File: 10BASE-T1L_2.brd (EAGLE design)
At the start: 60.8 x 75 mm, 163 parts, among them J1 10104110-0001LF, J2 A-2004-2-4-LPS-N-R, J3 TBL009-254-03GY-2GY, J4 TBL009-254-02GY-2GY, T1 ALT4532M-201-T001, T4 H1102NLT, U1 DP83TD510ERHBR, U2 DP83822IRHBR, U3 CO32H4-25.000-33GDTST, U4 LMR38020SDDAR, U5 SN74LVC1G17DCKR, U6 SN74LVC1G17DCKR

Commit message: adding reset cap
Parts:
- added C61: 10nF, ruark2:0402_INDUCTOR
- R68: value 100k -> 115k
- R69: value 24.9k -> 49.9k
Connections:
- net !RST: now also C61.P$1
- net GND: now also C61.P$2
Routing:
- net GND: track 73.3 -> 74.1 mm, vias 92 -> 97
- net !RST: track 24.1 -> 24.6 mm
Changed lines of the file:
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@@
 <attribute name="VALUE" x="11.684" y="11.176" size="1.27" layer="27"/>
 </element>
-<element name="R68" library="ruark2" package="0603" value="100k" x="5.842" y="31.496" smashed="yes" rot="R90">
+<element name="R68" library="ruark2" package="0603" value="115k" x="5.842" y="31.496" smashed="yes" rot="R90">
 <attribute name="NAME" x="5.08" y="30.226" size="1.016" layer="25" font="vector" ratio="10" rot="R90"/>
 <attribute name="VALUE" x="7.62" y="30.226" size="1.016" layer="27" font="vector" rot="R90"/>
 </element>
-<element name="R69" library="ruark2" package="0603" value="24.9k" x="5.842" y="34.798" smashed="yes" rot="R270">
+<element name="R69" library="ruark2" package="0603" value="49.9k" x="5.842" y="34.798" smashed="yes" rot="R270">
 <attribute name="NAME" x="5.08" y="33.782" size="1.016" layer="25" font="vector" ratio="10" rot="R90"/>
 <attribute name="VALUE" x="4.064" y="36.068" size="1.016" layer="27" font="vector" rot="R270"/>
@@
 </element>
 <element name="C30" library="ruark2" package="0402_INDUCTOR" value="47pF" x="43.434" y="15.748" smashed="yes" rot="R270">
-<attribute name="NAME" x="43.942" y="16.51" size="1.016" layer="25" font="vector" ratio="10" rot="R270"/>
+<attribute name="NAME" x="42.926" y="13.97" size="1.016" layer="25" font="vector" ratio="10" rot="R270"/>
 </element>
 <element name="L6" library="ruark2" package="TMPC0603H" value="22uH" x="6.858" y="19.812" smashed="yes" rot="R90">
@@
 <element name="C60" library="ruark2" package="0402_INDUCTOR" value="0.1uF" x="45.974" y="10.16" smashed="yes" rot="R90">
 <attribute name="NAME" x="47.498" y="8.89" size="1.016" layer="25" font="vector" rot="R90"/>
+</element>
+<element name="C61" library="ruark2" package="0402_INDUCTOR" value="10nF" x="42.926" y="27.94" smashed="yes" rot="R180">
+<attribute name="NAME" x="43.688" y="27.432" size="1.016" layer="25" font="vector" rot="R180"/>
 </element>
 </elements>
@@
 <wire x1="28.448" y1="22.098" x2="27.94" y2="22.606" width="0.4064" layer="1"/>
 <polygon width="0.1524" layer="1">
-<vertex x="6.604" y="68.58"/>
-<vertex x="6.604" y="54.356"/>
-<vertex x="3.048" y="54.356"/>
-<vertex x="3.048" y="68.58"/>
+<vertex x="6.604" y="69.342"/>
+<vertex x="6.604" y="53.086"/>
+<vertex x="3.048" y="53.086"/>
+<vertex x="3.048" y="69.342"/>
 </polygon>
 <contactref element="TP1" pad="P$1"/>
@@
 <wire x1="36.83" y1="7.882" x2="39.408" y2="7.882" width="0.180340625" layer="1"/>
 <wire x1="39.408" y1="7.882" x2="39.512" y2="7.986" width="0.180340625" layer="1"/>
+<contactref element="C61" pad="P$2"/>
+<wire x1="43.426" y1="27.94" x2="44.196" y2="27.94" width="0.180340625" layer="1"/>
+<via x="44.196" y="27.94" extent="1-16" drill="0.3048"/>
+<via x="3.556" y="53.594" extent="1-16" drill="0.3048"/>
+<via x="6.096" y="53.594" extent="1-16" drill="0.3048"/>
+<via x="6.096" y="68.834" extent="1-16" drill="0.3048"/>
+<via x="3.556" y="68.834" extent="1-16" drill="0.3048"/>
 </signal>
 <signal name="N$15">
@@
 <wire x1="45.428575" y1="22.86" x2="45.03674375" y2="23.25183125" width="0.180340625" layer="1"/>
 <wire x1="45.03674375" y1="24.77583125" x2="43.688" y2="26.124575" width="0.180340625" layer="1"/>
-<wire x1="43.688" y1="26.124575" x2="43.688" y2="26.924" width="0.180340625" layer="1"/>
-<via x="43.688" y="26.924" extent="1-16" drill="0.3048"/>
-<wire x1="43.688" y1="26.924" x2="42.418" y2="28.194" width="0.180340625" layer="16"/>
-<wire x1="42.418" y1="33.274" x2="42.418" y2="28.194" width="0.180340625" layer="16"/>
+<wire x1="43.688" y1="26.124575" x2="43.688" y2="26.416" width="0.180340625" layer="1"/>
+<via x="43.688" y="26.416" extent="1-16" drill="0.3048"/>
+<wire x1="43.688" y1="26.416" x2="42.418" y2="27.686" width="0.180340625" layer="16"/>
+<wire x1="42.418" y1="33.274" x2="42.418" y2="27.686" width="0.180340625" layer="16"/>
 <via x="42.418" y="33.274" extent="1-16" drill="0.3048"/>
 <wire x1="42.418" y1="33.274" x2="42.418" y2="34.282" width="0.180340625" layer="1"/>
@@
 <wire x1="46.422" y1="22.348" x2="45.47" y2="22.348" width="0.180340625" layer="1"/>
 <wire x1="45.47" y1="22.348" x2="44.704" y2="23.114" width="0.180340625" layer="1"/>
-<wire x1="44.704" y1="23.114" x2="44.704" y2="24.638" width="0.180340625" layer="1"/>
-<wire x1="44.704" y1="24.638" x2="41.402" y2="27.94" width="0.180340625" layer="1"/>
-<wire x1="41.402" y1="27.94" x2="38.1" y2="27.94" width="0.180340625" layer="1"/>
+<wire x1="44.704" y1="23.114" x2="44.704" y2="23.876" width="0.180340625" layer="1"/>
+<wire x1="44.704" y1="23.876" x2="40.64" y2="27.94" width="0.180340625" layer="1"/>
+<wire x1="40.64" y1="27.94" x2="38.1" y2="27.94" width="0.180340625" layer="1"/>
 <wire x1="38.1" y1="27.94" x2="37.592" y2="28.448" width="0.180340625" layer="1"/>
 <wire x1="37.592" y1="28.448" x2="37.592" y2="30.48" width="0.180340625" layer="1"/>
@@
 <wire x1="45.6434875" y1="23.348" x2="45.3694875" y2="23.622" width="0.180340625" layer="1"/>
 <wire x1="45.3694875" y1="23.622" x2="45.3694875" y2="26.2585125" width="0.180340625" layer="1"/>
-<wire x1="45.3694875" y1="26.2585125" x2="43.688" y2="27.94" width="0.180340625" layer="1"/>
-<wire x1="43.688" y1="27.94" x2="43.18" y2="27.94" width="0.180340625" layer="1"/>
-<wire x1="43.18" y1="27.94" x2="42.426" y2="28.694" width="0.180340625" layer="1"/>
-<wire x1="42.426" y1="28.694" x2="42.426" y2="29.21" width="0.180340625" layer="1"/>
 <wire x1="31.048" y1="23.348" x2="33.548" y2="23.348" width="0.180340625" layer="1"/>
 <wire x1="33.548" y1="23.348" x2="33.782" y2="23.114" width="0.180340625" layer="1"/>
@@
 <wire x1="39.624" y1="29.21" x2="42.426" y2="29.21" width="0.180340625" layer="1"/>
 <wire x1="37.338" y1="26.924" x2="39.624" y2="29.21" width="0.180340625" layer="16"/>
+<contactref element="C61" pad="P$1"/>
+<wire x1="45.3694875" y1="26.2585125" x2="44.45" y2="27.178" width="0.180340625" layer="1"/>
+<wire x1="43.02511875" y1="27.178" x2="42.426" y2="27.77711875" width="0.180340625" layer="1"/>
+<wire x1="42.426" y1="27.77711875" x2="42.426" y2="27.94" width="0.180340625" layer="1"/>
+<wire x1="44.45" y1="27.178" x2="43.02511875" y2="27.178" width="0.180340625" layer="1"/>
+<wire x1="42.426" y1="27.94" x2="42.426" y2="29.21" width="0.180340625" layer="1"/>
 </signal>
 <signal name="N$2">

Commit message: Added PD detection
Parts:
- removed R65: 75, ruark2:0603
- added C62: 0.1uF, ruark2:0402_INDUCTOR
- added D11, D12: (no value), diode:MINIMELF
- added D5, D7, D8: SM4007PL, ruark2:SOD123(AK)
- added D9: CJ431, ruark2:SOT23-3_CENTERED
- added Q1, Q2, Q3: MMBT5551, ruark2:SOT23-3_CENTERED
- added Q4: MMBT5401, ruark2:SOT23-3_CENTERED
- added Q5: AO3400A, ruark2:SOT23-3_CENTERED
- added R60, R63: 75, ruark2:R0402
- added R71, R72, R73, R74: 1M, ruark2:0603
- added R75: 10k, ruark2:R0402
- added R76: 100k, ruark2:R0402
- added R77, R79: 1M, ruark2:R0402
- added R80: 10M, ruark2:R0402
- R32, R33: device ruark2:0603 -> ruark2:R0402
- R64: value 75 -> 0R; device ruark2:0603 -> ruark2:1206
- moved R64 36.1 mm to (11.2, 48.0), turned to 180 degrees
- moved R33 9.30 mm to (52.7, 54.6), turned to 90 degrees
- moved R32 3.76 mm to (46.4, 54.6), turned to 90 degrees
- moved D6 3.05 mm to (20.1, 57.9)
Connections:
- removed net RX+: J2.3, T4.11
- removed net RX-: J2.6, T4.9
- removed net TX+: J2.1, T4.16
- removed net TX-: J2.2, T4.14
- new net N$11: Q4.3, R75.2
- new net N$20: D9.1, R73.1, R74.2
- new net N$21: D7.K, D8.K, F1.1
- new net N$28: Q3.1, R75.1, R76.2
- new net N$35: Q1.3, Q4.1, R71.1
- new net N$39: Q1.1, Q2.3, R72.1
- new net N$41: D11.A, R77.2, R79.1, R80.2
- new net N$44: Q2.1, R79.2
- new net N$45: D12.C, Q5.1, R77.1
- new net N$7: C62.P$2, D9.3, Q3.3, R74.1
- new net N$8: C14.1, D5.K, D8.A, L1.OUT2
- new net RTN: D5.A, D6.A, Q1.2, Q2.2, Q3.2, Q5.3, R76.1, R80.1
- new net RX_N: J2.2, T4.9
- new net RX_P: J2.1, T4.11
- new net TX_N: J2.6, T4.14
- new net TX_P: J2.3, T4.16
- new net V+R: C17.1, C38.1, C39.1, C40.1, C41.1, C42.1, C43.1, C44.1, C45.1, C46.1, C50.1, C51.1, C52.1, R64.2, R66.2, U4.3
- net BS: now also R60.1, R63.1; no longer R64.1, R65.1
- net GND: now also D12.A, Q5.2; no longer C14.1, D6.A, L1.OUT2
- net N$26: now also D7.A; no longer F1.1
- net N$29: now also R32.1; no longer R64.2
- net N$4: now also R63.2; no longer R32.1
- net N$5: now also R60.2; no longer R33.1
- net N$64: now also R33.1; no longer R65.2
- net V+: now also C62.P$1, D11.C, D9.2, Q4.2, R64.1, R71.2, R72.2, R73.2; no longer C17.1, C38.1, C39.1, C40.1, C41.1, C42.1, C43.1, C44.1, C45.1, C46.1, C50.1, C51.1, C52.1, R66.2, U4.3
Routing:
- net V+: track 41.5 -> 15.6 mm
- net N$8: track 0.00 -> 23.3 mm, vias 0 -> 3
- net RX+: track 19.2 -> 0.00 mm, vias 1 -> 0
- net TX_P: track 0.00 -> 15.5 mm
- net TX_N: track 0.00 -> 15.0 mm
- net V+R: track 0.00 -> 15.0 mm, vias 0 -> 2
- net RX-: track 13.8 -> 0.00 mm, vias 1 -> 0
- net RX_P: track 0.00 -> 13.5 mm
- net TX+: track 13.4 -> 0.00 mm
- net RX_N: track 0.00 -> 13.0 mm
- net TX-: track 8.93 -> 0.00 mm
- net N$4: track 18.0 -> 9.26 mm
- net N$21: track 0.00 -> 4.77 mm
- net GND: track 74.1 -> 70.1 mm, vias 97 -> 94
- net N$17: track 14.5 -> 11.1 mm
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- added copper zone on layer 1, net V+R
- removed copper zone on layer 1, net V+

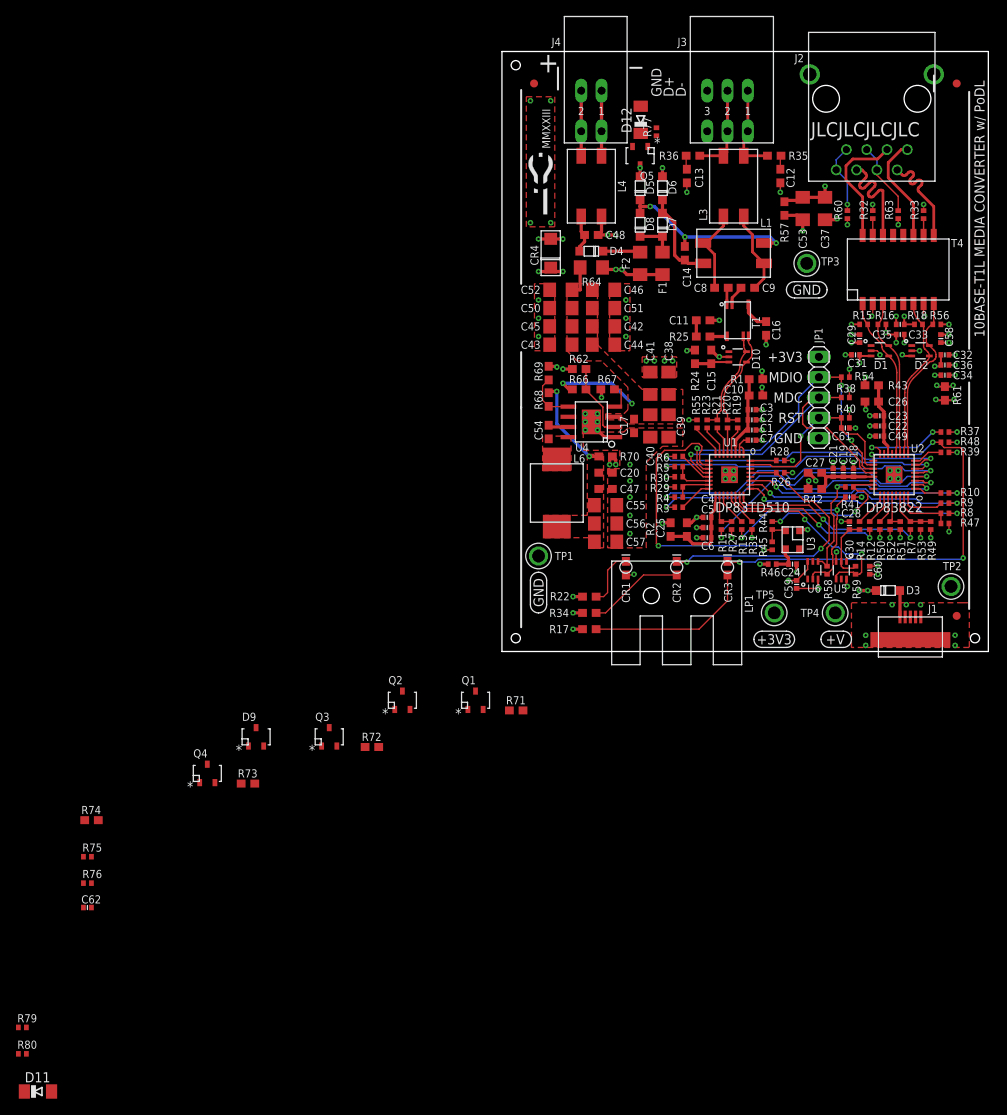
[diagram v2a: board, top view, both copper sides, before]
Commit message: Rev2
Fixed RGMII clock
Fixed LED package
Fixed 3.3V PoL output voltage
Fixed oscillator footprint
Fixed PoDl
Switched to JLC Available connectors
Fixed common mode chokes.
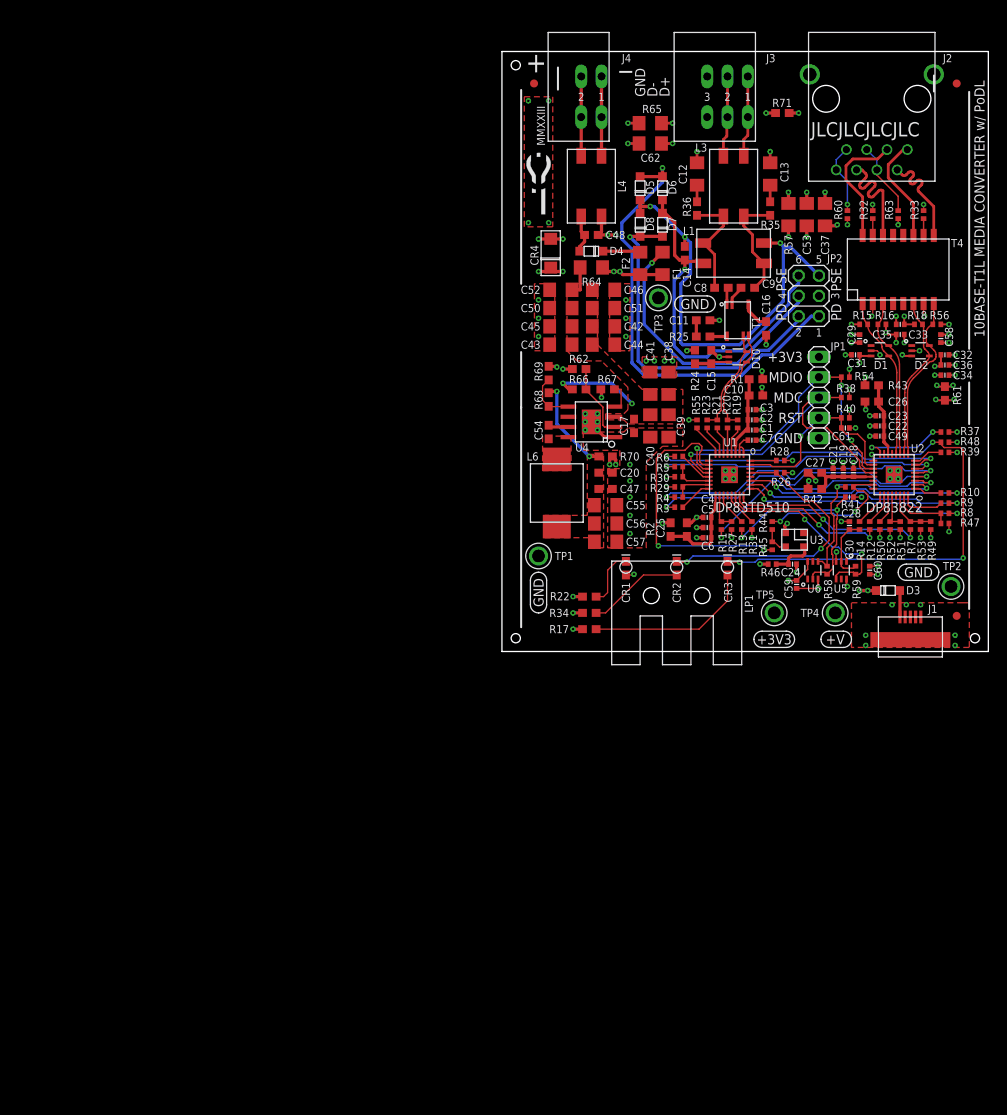
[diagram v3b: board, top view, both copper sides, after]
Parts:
- removed D11, D12: (no value), diode:MINIMELF
- removed D9: CJ431, ruark2:SOT23-3_CENTERED
- removed Q1, Q2, Q3: MMBT5551, ruark2:SOT23-3_CENTERED
- removed Q4: MMBT5401, ruark2:SOT23-3_CENTERED
- removed Q5: AO3400A, ruark2:SOT23-3_CENTERED
- removed R72, R73, R74: 1M, ruark2:0603
- removed R75: 10k, ruark2:R0402
- removed R76: 100k, ruark2:R0402
- removed R77, R79: 1M, ruark2:R0402
- removed R80: 10M, ruark2:R0402
- added JP2: (no value), pinhead:2X03
- added R65: 1M, ruark2:1206
- C12, C13: value 0.1uF -> 1nF 1kV; device ruark2:0603 -> rcl:C1206
- C62: value 0.1uF -> 1nF 1kV; device ruark2:0402_INDUCTOR -> rcl:C1206
- J3: value TBL009-254-03GY-2GY -> KF141R-2.54-3P; device ruark2:TBL009-254-03GY-2GY -> ruark2:KF141R-2.54-3P
- J4: value TBL009-254-02GY-2GY -> KF141R-2.54-2P; device ruark2:TBL009-254-02GY-2GY -> ruark2:KF141R-2.54-2P
- R22: value 499 -> 470
- R32, R33, R60, R63: value 75 -> 49.9
- R50: value 1.96k -> 2k
- R51: value 6.2k -> 5.1k
- R52: value 1.96k -> 1.5k
- R57: device ruark2:0603 -> ruark2:1206
- R62: value 750k -> 100k
- R66: value 1.65M -> 220k
- R67: value 64.9k -> 68k
- R68: value 115k -> 22k
- R69: value 49.9k -> 51k
- R71: value 1M -> DNP
- moved C62 118.6 mm to (18.5, 63.5), turned to 180 degrees
- moved R71 81.8 mm to (35.1, 67.3)
- moved TP3 19.0 mm to (19.6, 44.2)
- moved C12 10.4 mm to (24.4, 59.7)
- moved C13 10.4 mm to (33.5, 59.7)
- moved R35 6.62 mm to (33.5, 55.4), turned to 270 degrees
- moved R36 6.62 mm to (24.4, 55.4), turned to 270 degrees
- moved J3 1.78 mm to (28.2, 69.3)
- moved C53 0.92 mm to (38.1, 54.6)
- moved R57 0.92 mm to (35.8, 54.6)
- moved C37 0.76 mm to (40.4, 54.6)
- moved J4 0.76 mm to (11.2, 69.3)
- moved U3 0.25 mm to (36.6, 14.0), turned to 180 degrees
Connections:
- removed net N$11: Q4.3, R75.2
- removed net N$20: D9.1, R73.1, R74.2
- removed net N$21: D7.K, D8.K, F1.1
- removed net N$26: C14.2, D6.K, D7.A, L1.IN1
- removed net N$28: Q3.1, R75.1, R76.2
- removed net N$35: Q1.3, Q4.1, R71.1
- removed net N$39: Q1.1, Q2.3, R72.1
- removed net N$41: D11.A, R77.2, R79.1, R80.2
- removed net N$44: Q2.1, R79.2
- removed net N$45: D12.C, Q5.1, R77.1
- removed net N$7: C62.P$2, D9.3, Q3.3, R74.1
- removed net N$8: C14.1, D5.K, D8.A, L1.OUT2
- new net EARTH: C11.1, C12.2, C13.2, C62.1, J3.3A, J3.3B, R65.2, R71.1
- new net IN+: C14.2, D6.K, D7.A, JP2.6, L1.IN1
- new net IN-: C14.1, D5.K, D8.A, JP2.5, L1.OUT2
- new net V+F: F1.1, JP2.4
- new net VIN: D7.K, D8.K, JP2.2
- net CGND: now also R71.2
- net GND: now also C62.2, JP2.3, R65.1; no longer C11.1, C12.1, C13.1, D12.A, J3.3A, J3.3B, Q5.2
- net N$17: now also R36.2
- net N$18: now also R35.2
- net N$36: no longer R35.2
- net N$42: now also C12.1; no longer C13.2
- net N$48: now also C13.1; no longer C12.2
- net N$49: no longer R36.2
- net RTN: now also JP2.1; no longer Q1.2, Q2.2, Q3.2, Q5.3, R76.1, R80.1
- net V+: no longer C62.P$1, D11.C, D9.2, Q4.2, R71.2, R72.2, R73.2
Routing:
- net RTN: track 2.43 -> 57.9 mm, vias 2 -> 1
- net IN-: track 0.00 -> 54.6 mm, vias 0 -> 3
- net IN+: track 0.00 -> 44.7 mm, vias 0 -> 1
- net VIN: track 0.00 -> 43.4 mm, vias 0 -> 1
- net V+F: track 0.00 -> 35.3 mm, vias 0 -> 1
- net N$8: track 23.3 -> 0.00 mm, vias 3 -> 0
- net N$26: track 11.7 -> 0.00 mm
- net EARTH: track 0.00 -> 7.94 mm, vias 0 -> 6
- net N$21: track 4.77 -> 0.00 mm
- net N$18: track 10.4 -> 13.9 mm
- net N$17: track 11.1 -> 14.2 mm
- net N$62: track 3.55 -> 5.44 mm
- net N$34: track 8.14 -> 9.92 mm
- net N$12: track 8.14 -> 9.92 mm
- net GND: track 70.1 -> 68.4 mm
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- added copper zone on layer 15, net EARTH
- added copper zone on layer 2, net EARTH
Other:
- board text added: "1"
- board text added: "2"
- board text added: "3"
- board text added: "4"
- board text added: "5"
- board text added: "6"
- board text added: "PD"
- board text added: "PSE"
